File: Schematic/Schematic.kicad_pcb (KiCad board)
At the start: 2 copper layers, 115.3 x 171.4 mm, 138 parts, among them J1 HUB75_DATA, J10 Conn_01x03_Pin, J11 Conn_01x03_Pin, J12 Conn_01x03_Pin, J13 Conn_01x03_Pin, J14 WS2812B_DATA, J15 WS2812B_PWR, J16 Conn_01x03_Pin, J17 Conn_01x05_Pin, J18 LASER, J19 LDR, J2 KEYPAD, J3 HUB75_PWR, J4 AUDIO_OUT, J5 DEBUG_HEADER, J6 Conn_01x03_Pin, J7 Conn_01x03_Pin, J8 Conn_01x03_Pin, J9 Conn_01x03_Pin, SW1 RESET, U1 74LS08, U2 STM32F091RCT6, U3 LM386, U4 LM2678S-12, U5 LD1117S33TR_SOT223, U6 MAX7375AXR805, U7 LM358, U8 SN74AHCT125N

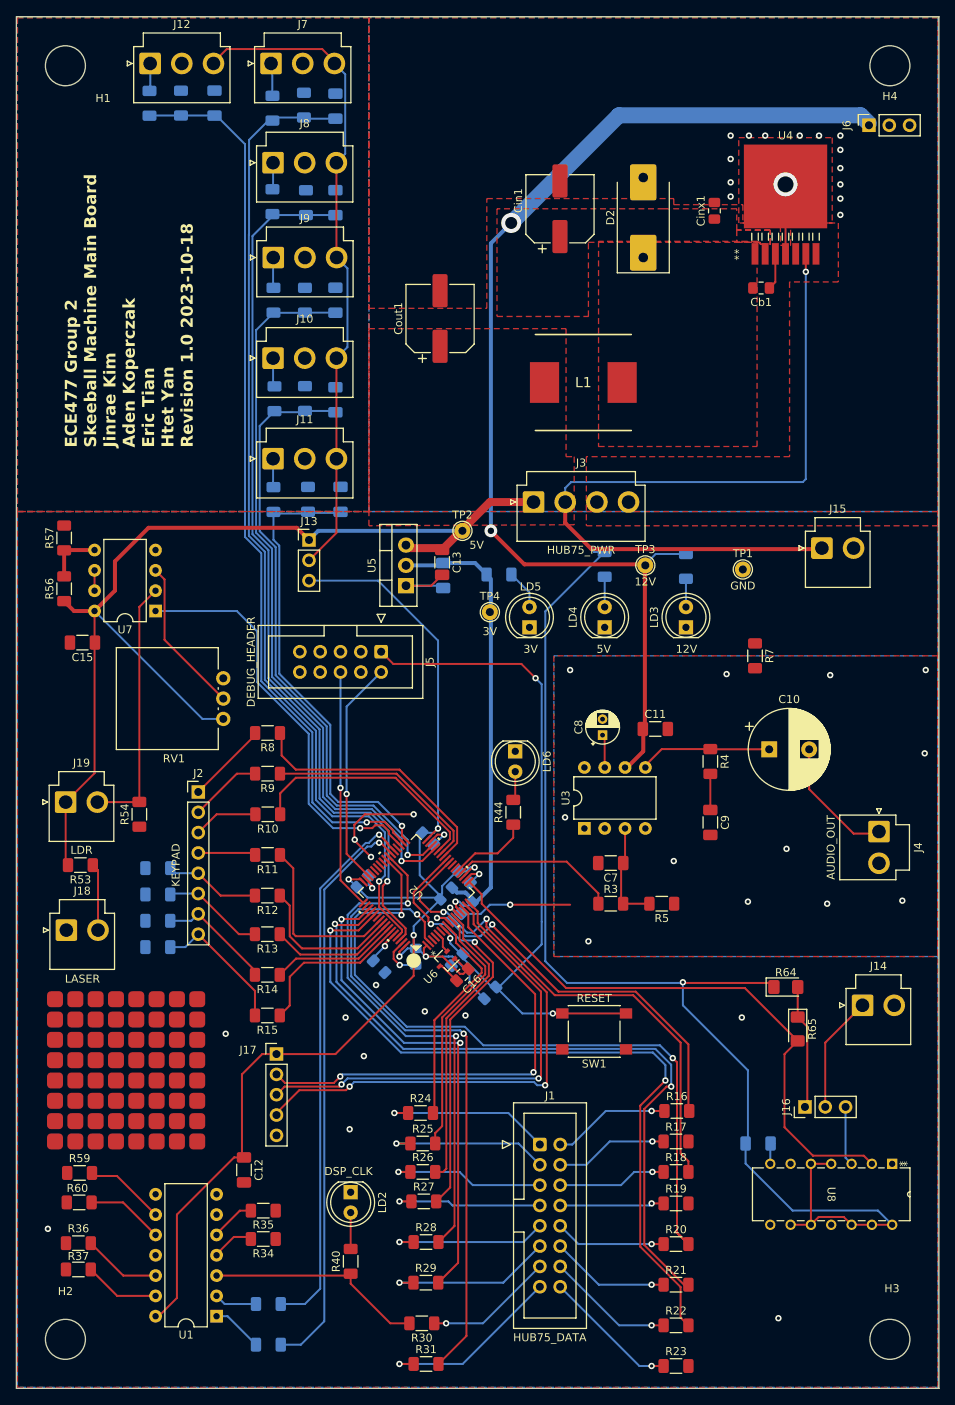
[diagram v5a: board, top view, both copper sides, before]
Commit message: relabeld all of the components so they have more resonable numbers
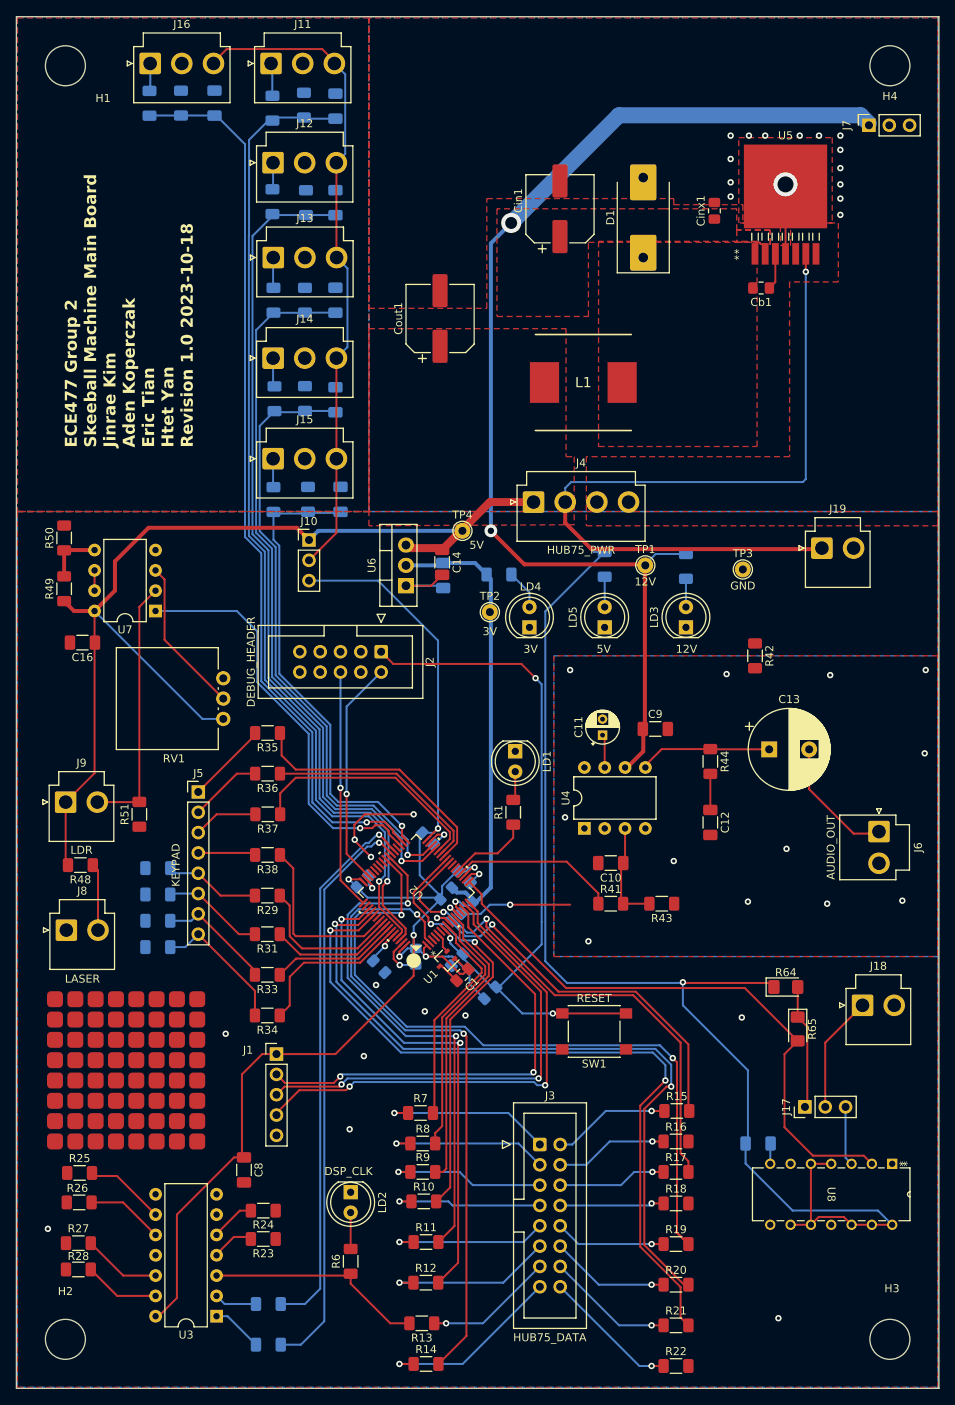
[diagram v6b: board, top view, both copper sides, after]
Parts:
- renumbered C16 to C1, C7 to C10, C8 to C11, C9 to C12, C10 to C13, C13 to C14, C14 to C15, C15 to C16, C22 to C17, C21 to C18, C20 to C19, C19 to C20, C18 to C21, C17 to C22, C1 to C5, C5 to C6, C6 to C7, C12 to C8, C11 to C9, D2 to D1, J17 to J1, J13 to J10, J7 to J11, J8 to J12, J9 to J13, J10 to J14, J11 to J15, J12 to J16, J16 to J17, J14 to J18, J15 to J19, J5 to J2, J1 to J3, J3 to J4, J2 to J5, J4 to J6, J6 to J7, J18 to J8, J19 to J9, LD6 to LD1, LD5 to LD4, LD4 to LD5, R44 to R1, R27 to R10, R28 to R11, R29 to R12, R30 to R13, R31 to R14, R16 to R15, R17 to R16, R18 to R17, R19 to R18, R20 to R19, R21 to R20, R22 to R21, R23 to R22, R34 to R23, R35 to R24, R59 to R25, R60 to R26, R36 to R27, R37 to R28, R12 to R29, R1 to R3, R63 to R30, R13 to R31, R62 to R32, R14 to R33, R15 to R34, R8 to R35, R9 to R36, R10 to R37, R11 to R38, R61 to R39, R32 to R4, R6 to R40, R3 to R41, R7 to R42, R5 to R43, R4 to R44, R41 to R45, R43 to R46, R42 to R47, R53 to R48, R56 to R49, R33 to R5, R57 to R50, R54 to R51, R38 to R52, R39 to R53, R45 to R54, R46 to R55, R47 to R56, R48 to R57, R49 to R58, R50 to R59, R40 to R6, R51 to R60, R52 to R61, R55 to R62, R58 to R63, R24 to R7, R25 to R8, R26 to R9, TP3 to TP1, TP4 to TP2, TP1 to TP3, TP2 to TP4, U6 to U1, U1 to U3, U3 to U4, U4 to U5, U5 to U6
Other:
- rule pad_to_mask_clearance: 0 -> 0.038

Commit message: fixed LM385 not having voltage div, and ploted plots.
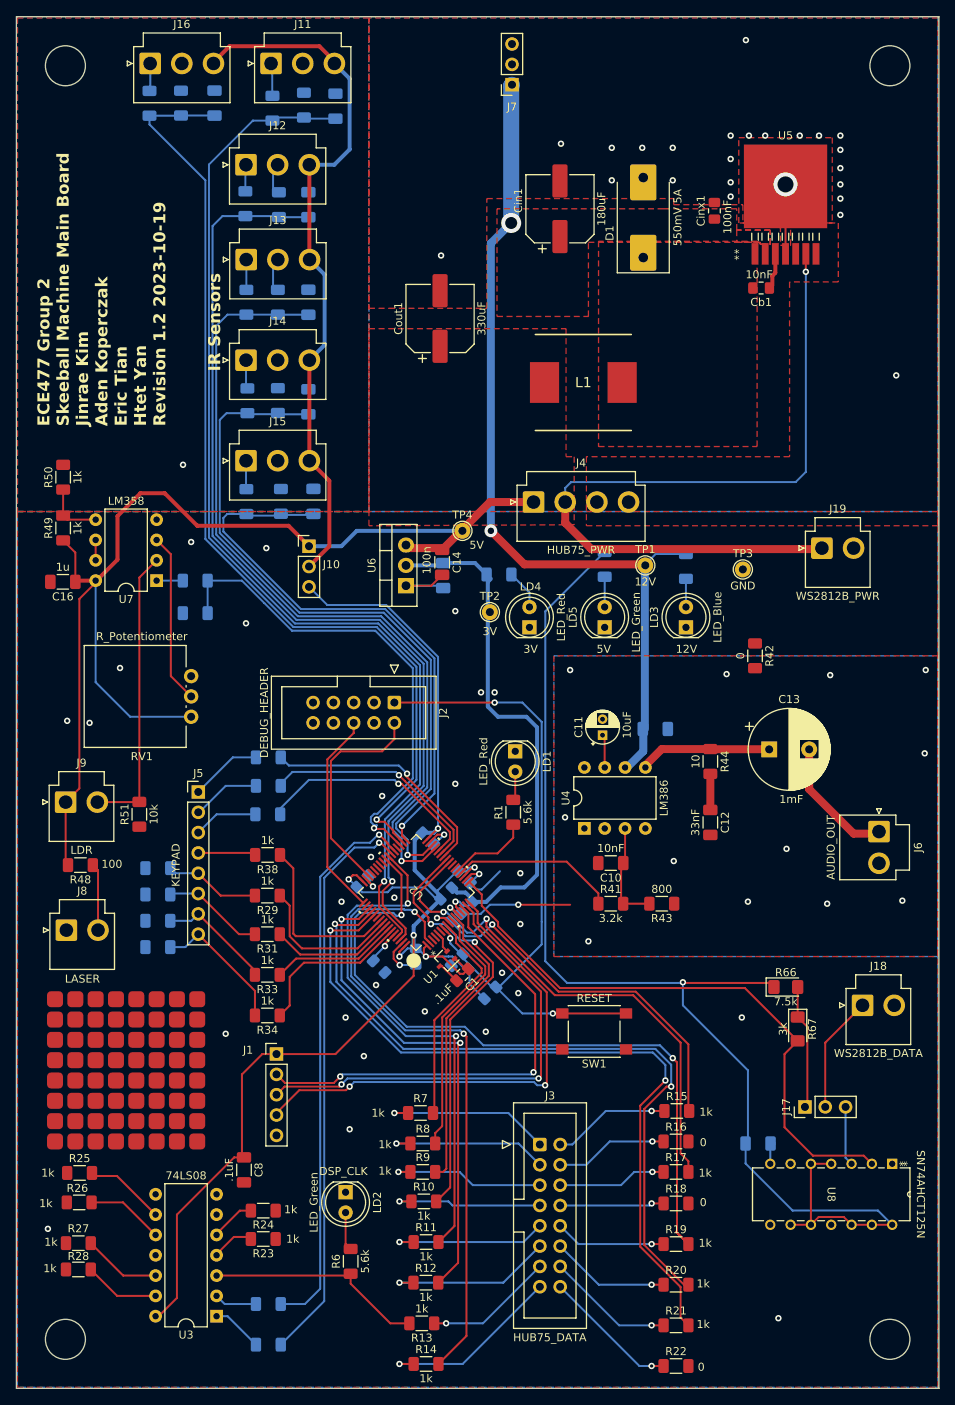
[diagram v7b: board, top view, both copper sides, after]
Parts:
- added R52: 1k, Resistor_SMD:R_1206_3216Metric_Pad1.30x1.75mm_HandSolder, B.Cu at (58.2, 94.0)
- added R53: 2k, Resistor_SMD:R_1206_3216Metric_Pad1.30x1.75mm_HandSolder, B.Cu at (58.2, 98.0)
- C9, R35, R36, R37: moved to B.Cu
- moved J7 44.9 mm to (97.8, 32.0), turned to 180 degrees
- moved C16 7.98 mm to (41.6, 94.1)
- moved R49 7.60 mm to (41.7, 87.4)
- moved R50 7.60 mm to (41.7, 81.1)
- moved J2 6.56 mm to (83.1, 109.2)
- moved RV1 4.02 mm to (57.7, 105.9)
- moved U7 3.80 mm to (53.3, 94.0)
- moved R57 3.39 mm to (64.7, 71.5)
- moved R62 3.39 mm to (68.5, 59.2)
- moved R64 3.39 mm to (68.9, 84.1)
- moved J12 3.39 mm to (64.5, 42.0)
- moved R63 3.39 mm to (68.5, 71.5)
- moved C18 3.39 mm to (72.3, 47.0)
- moved C19 3.39 mm to (72.3, 59.2)
- moved C20 3.39 mm to (72.3, 71.6)
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- renumbered R52 to R54, R53 to R55, R54 to R56, R55 to R57, R56 to R58, R57 to R59, R58 to R60, R59 to R61, R60 to R62, R61 to R63, R62 to R64, R63 to R65, R64 to R66, R65 to R67
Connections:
- U7 pad 1: PB14 -> Net-(R52-Pad2)
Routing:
- net +12V: track 143.5 -> 109.5 mm
- net +5V: track 392.3 -> 408.6 mm
- net PB8: track 123.1 -> 135.4 mm
- net PB9: track 110.7 -> 122.8 mm
- net PB12: track 59.0 -> 70.8 mm
- net PB11: track 77.9 -> 89.0 mm
- net PB10: track 92.2 -> 103.2 mm
- net PB13: track 112.8 -> 122.8 mm
- net Vin: track 61.0 -> 70.7 mm
- net PB14: track 52.0 -> 61.4 mm
- net /microprocessor/NRST: track 90.2 -> 83.2 mm
- net /Sensors/Vsens: track 82.6 -> 88.4 mm
- net /microprocessor/SWCLK_IN: track 30.0 -> 25.7 mm, vias 1 -> 0
- net Net-(J9-Pin_2): track 32.5 -> 36.4 mm
- net Net-(R52-Pad2): track 0.00 -> 3.28 mm
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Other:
- rule pad_to_mask_clearance: 0.038 -> 0
- board text added: "ECE477 Group 2 Skeeball Machine Main Board Jinrae Kim​ Aden Koperczak​ Eric Tian​ Htet Yan​ Revision 1.2 2023-10-19"
- board text added: "Feedback Trace (not output)"
- board text added: "IR Sensors"
- board text added: "Vsw (Buck Output)"
- board text removed: "ECE477 Group 2 Skeeball Machine Main Board Jinrae Kim​ Aden Koperczak​ Eric Tian​ Htet Yan​ Revision 1.0 2023-10-18"
